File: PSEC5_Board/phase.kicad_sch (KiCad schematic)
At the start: 8 parts, among them U4 SN74LVC1G97DBVTG4, U6 OPA607QDBVRQ1, U7 AD4008BCPZ-RL7, Y1 ASE2-40.000MHZ-ET

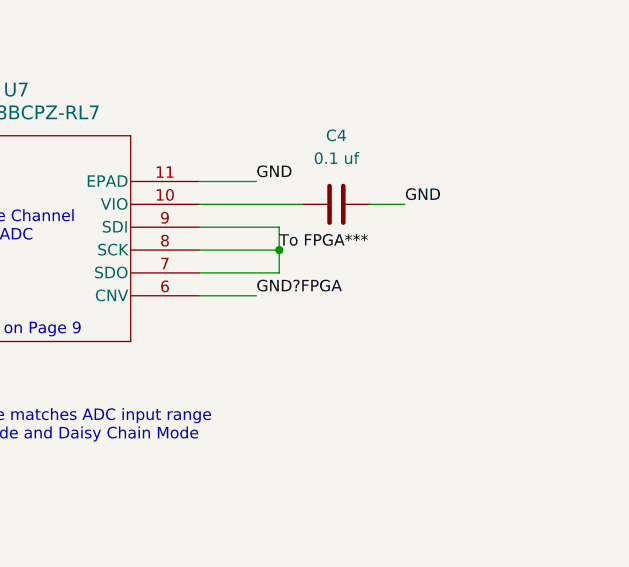
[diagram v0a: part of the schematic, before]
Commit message: DUT Push: ADC Buffer, PLL changes
Implemented ADC Buffer (x1), adjusted PLL ADC.

Missing: PLL DAC, SAMTEC and housekeeping
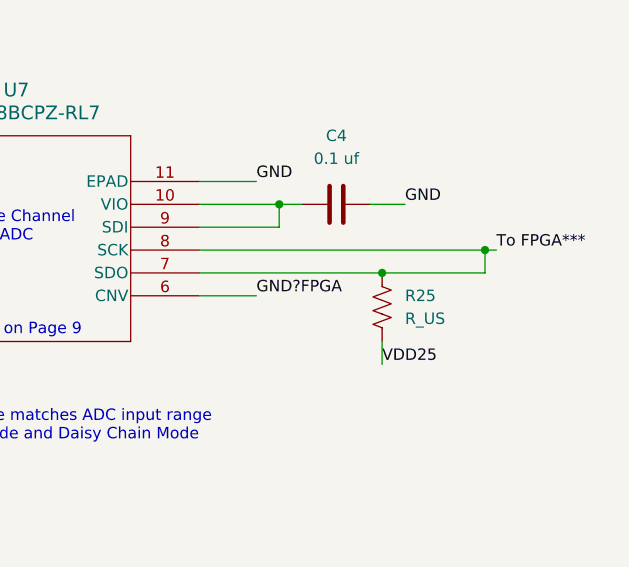
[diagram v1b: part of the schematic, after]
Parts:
- added R25: R_US, symbol Device:R_US
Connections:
- net To FPGA***: now also R25.2; no longer U7.9 (SDI)
- net VDD25: now also R25.1
- net at C4.2, U7.10 (VIO): now also U7.9 (SDI)
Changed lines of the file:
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@@
 	)
 	(junction
-		(at 240.03 91.44)
+		(at 262.89 91.44)
 		(diameter 0)
 		(color 0 0 0 0)
@@
 	)
 	(junction
+		(at 251.46 93.98)
+		(diameter 0)
+		(color 0 0 0 0)
+	)
+	(junction
+		(at 240.03 86.36)
+		(diameter 0)
+		(color 0 0 0 0)
+	)
+	(junction
 		(at 78.74 106.68)
 		(diameter 0)
@@
 	(wire
 		(pts
-			(xy 231.14 86.36) (xy 242.57 86.36)
+			(xy 231.14 86.36) (xy 240.03 86.36)
 		)
 		(stroke
@@
 	(wire
 		(pts
+			(xy 231.14 91.44) (xy 262.89 91.44)
+		)
+		(stroke
+			(width 0)
+			(type default)
+		)
+	)
+	(wire
+		(pts
 			(xy 76.2 106.68) (xy 78.74 106.68)
 		)
@@
 	(wire
 		(pts
-			(xy 240.03 88.9) (xy 240.03 91.44)
-		)
-		(stroke
-			(width 0)
-			(type default)
-		)
-	)
-	(wire
-		(pts
 			(xy 102.87 27.94) (xy 110.49 27.94)
 		)
@@
 	(wire
 		(pts
+			(xy 251.46 93.98) (xy 262.89 93.98)
+		)
+		(stroke
+			(width 0)
+			(type default)
+		)
+	)
+	(wire
+		(pts
 			(xy 179.07 93.98) (xy 190.5 93.98)
 		)
@@
 	(wire
 		(pts
+			(xy 264.16 91.44) (xy 262.89 91.44)
+		)
+		(stroke
+			(width 0)
+			(type default)
+		)
+	)
+	(wire
+		(pts
 			(xy 106.68 147.32) (xy 109.22 147.32)
 		)
@@
 	(wire
 		(pts
-			(xy 231.14 93.98) (xy 240.03 93.98)
+			(xy 231.14 93.98) (xy 251.46 93.98)
 		)
 		(stroke
@@
 	(wire
 		(pts
-			(xy 240.03 93.98) (xy 240.03 91.44)
+			(xy 262.89 91.44) (xy 262.89 93.98)
 		)
 		(stroke
@@
 	(wire
 		(pts
+			(xy 251.46 101.6) (xy 251.46 104.14)
+		)
+		(stroke
+			(width 0)
+			(type default)
+		)
+	)
+	(wire
+		(pts
 			(xy 64.77 166.37) (xy 64.77 153.67)
 		)
@@
 	(wire
 		(pts
+			(xy 240.03 88.9) (xy 240.03 86.36)
+		)
+		(stroke
+			(width 0)
+			(type default)
+		)
+	)
+	(wire
+		(pts
 			(xy 62.23 106.68) (xy 68.58 106.68)
 		)
@@
 	(wire
 		(pts
+			(xy 240.03 86.36) (xy 242.57 86.36)
+		)
+		(stroke
+			(width 0)
+			(type default)
+		)
+	)
+	(wire
+		(pts
 			(xy 97.79 92.71) (xy 102.87 92.71)
 		)
@@
 		(pts
 			(xy 179.07 88.9) (xy 190.5 88.9)
-		)
-		(stroke
-			(width 0)
-			(type default)
-		)
-	)
-	(wire
-		(pts
-			(xy 231.14 91.44) (xy 240.03 91.44)
 		)
 		(stroke
@@
 		)
 	)
+	(label "VDD25"
+		(at 251.46 104.14 0)
+		(fields_autoplaced yes)
+		(effects
+			(font
+				(size 1.27 1.27)
+			)
+			(justify left bottom)
+		)
+	)
 	(label "VDD18?"
 		(at 182.88 86.36 0)
@@
 	)
 	(label "To FPGA***"
-		(at 240.03 91.44 0)
-		(fields_autoplaced yes)
-		(effects
-			(font
-				(size 1.27 1.27)
-			)
-			(justify left bottom)
-		)
-	)
+		(at 264.16 91.44 0)
+		(fields_autoplaced yes)
+		(effects
+			(font
+				(size 1.27 1.27)
+			)
+			(justify left bottom)
+		)
+	)
+	(symbol
+		(lib_id "Device:R_US")
+		(at 251.46 97.79 180)
+		(unit 1)
+		(exclude_from_sim no)
+		(in_bom yes)
+		(on_board yes)
+		(dnp no)
+		(fields_autoplaced yes)
+		(property "Reference" "R25"
+			(at 254 96.5199 0)
+			(effects
+				(font
+					(size 1.27 1.27)
+				)
+				(justify right)
+			)
+		)
+		(property "Value" "R_US"
+			(at 254 99.0599 0)
+			(effects
+				(font
+					(size 1.27 1.27)
+				)
+				(justify right)
+			)
+		)
+		(property "Footprint" ""
+			(at 250.444 97.536 90)
+			(effects
+				(font
+					(size 1.27 1.27)
+				)
+				(hide yes)
+			)
+		)
+		(property "Datasheet" "~"
+			(at 251.46 97.79 0)
+			(effects
+				(font
+					(size 1.27 1.27)
+				)
+				(hide yes)
+			)
+		)
+		(property "Description" "Resistor, US symbol"
+			(at 251.46 97.79 0)
+			(effects
+				(font
+					(size 1.27 1.27)
+				)
+				(hide yes)
+			)
+		)
+		(pin "2"
+		)
+		(pin "1"
+		)
+		(instances
+			(project ""
+				(path "/af906810-6e6b-406e-b884-20eae48a7386/342f9d5e-3615-4623-a80b-f03a940e5896"
+					(reference "R25")
+					(unit 1)
+				)
+			)
+		)
+	)

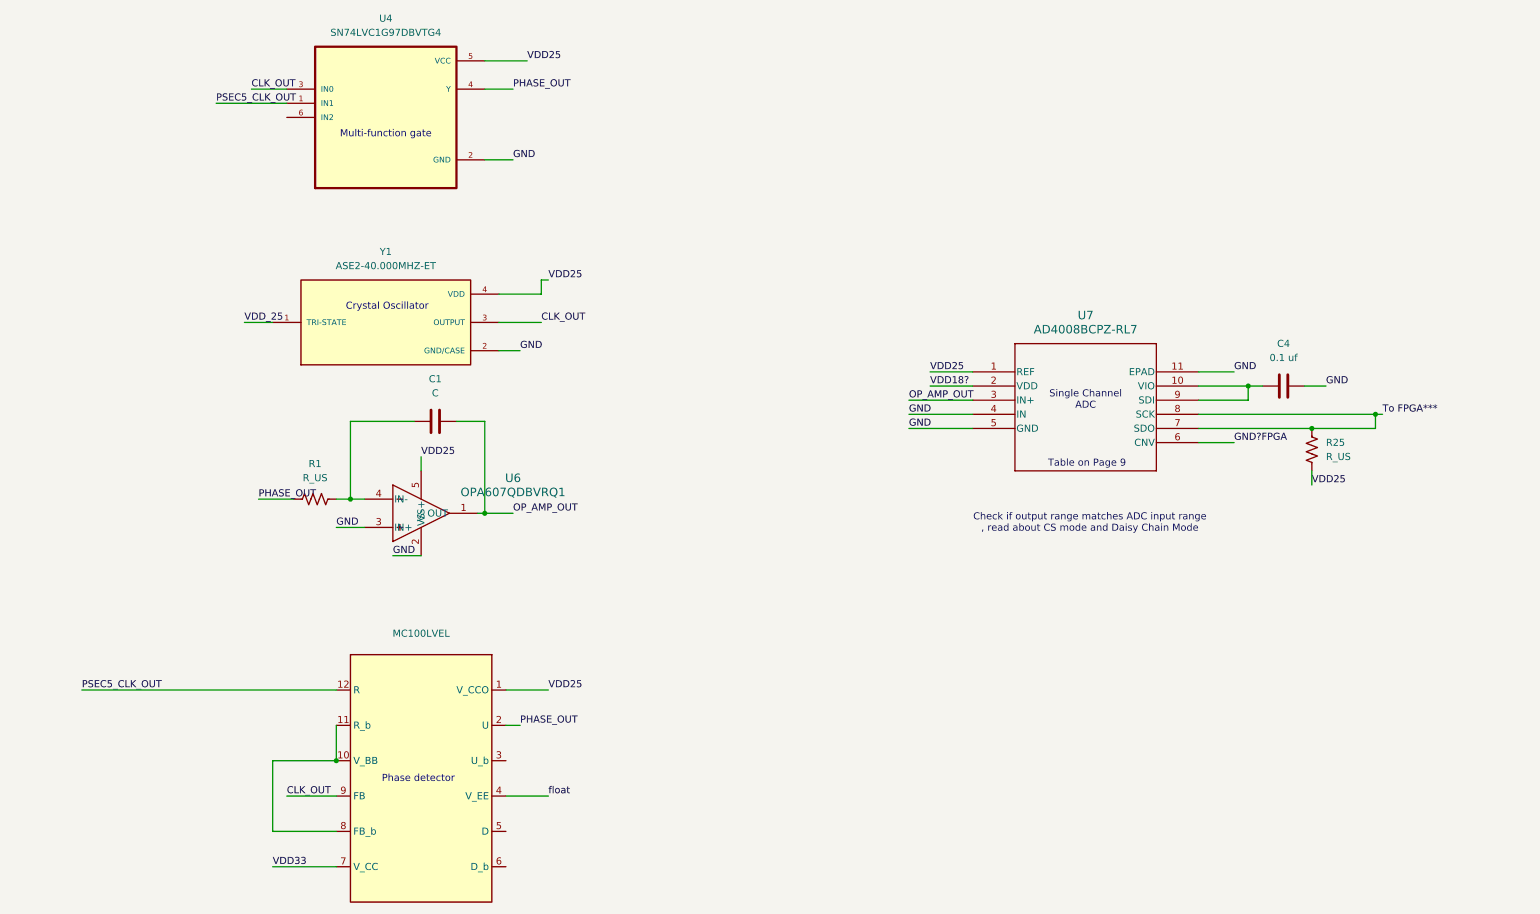
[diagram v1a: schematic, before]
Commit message: DUT Schematic Push
Very close -> Still need to convert to Sheet pins.

Added a second SAMTEC.
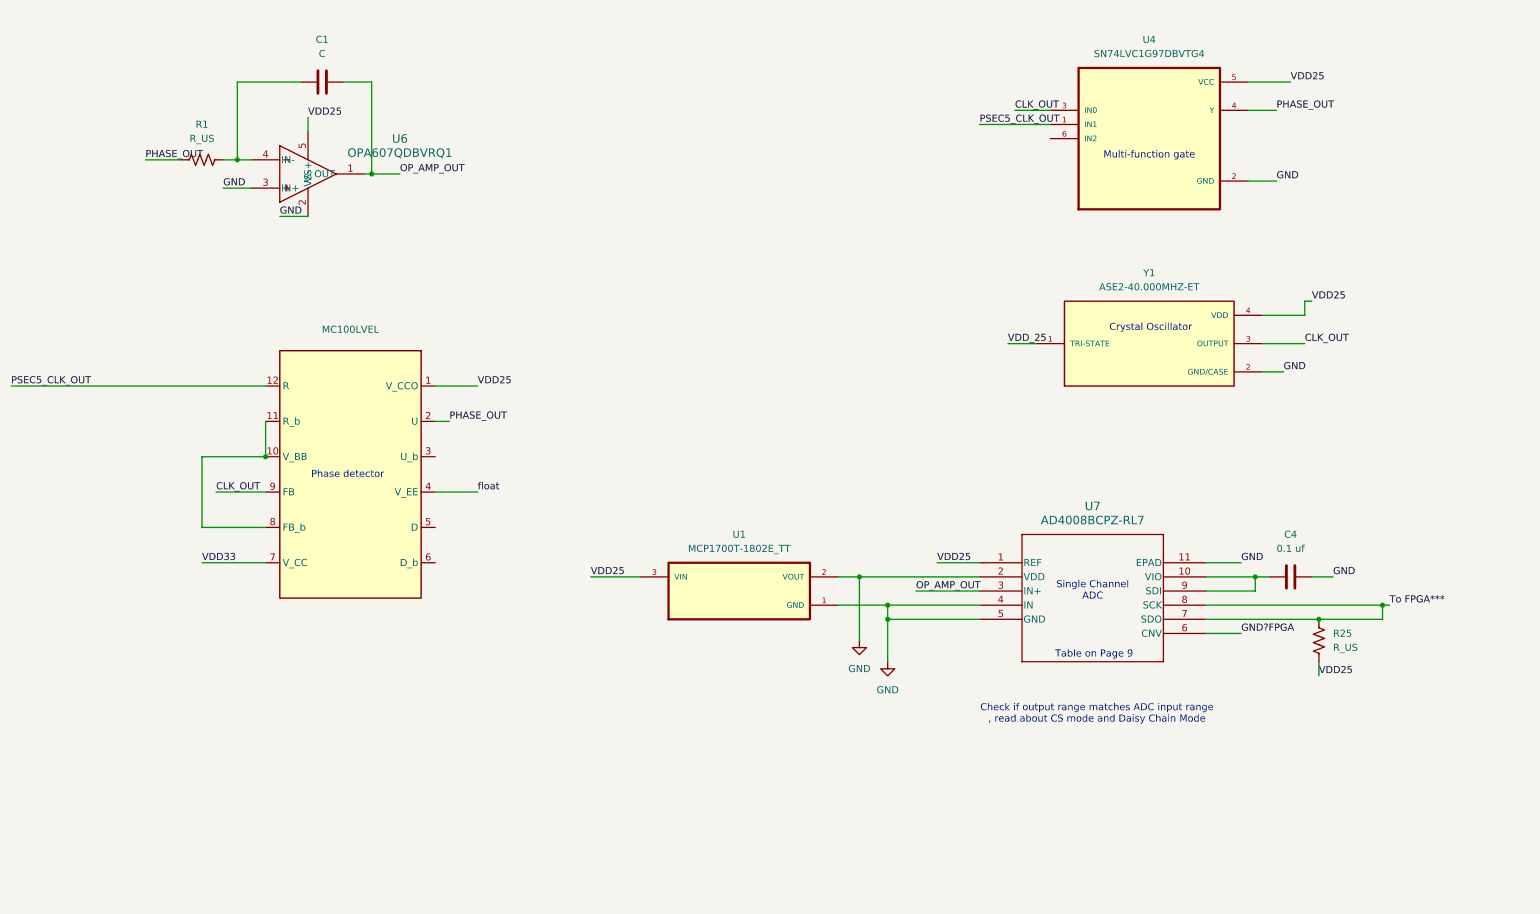
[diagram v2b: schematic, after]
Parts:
- added U1: MCP1700T-1802E_TT, MCP1700T-1802E_TT:SOT95P237X112-3N, symbol MCP1700T-1802E_TT:MCP1700T-1802E_TT
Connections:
- net VDD18? is gone; now on net GND: U7.2 (VDD)
- net GND: now also U1.1 (GND), U1.2 (VOUT)
- net VDD25: now also U1.3 (VIN)
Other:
- moved on the sheet: C1, C4, MC100LVEL, R1, R25, U4, U6, U7, Y1

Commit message: DUT - Fixed ADC Driver
Passes ERC - SAMTEC connections still needs to be matched.
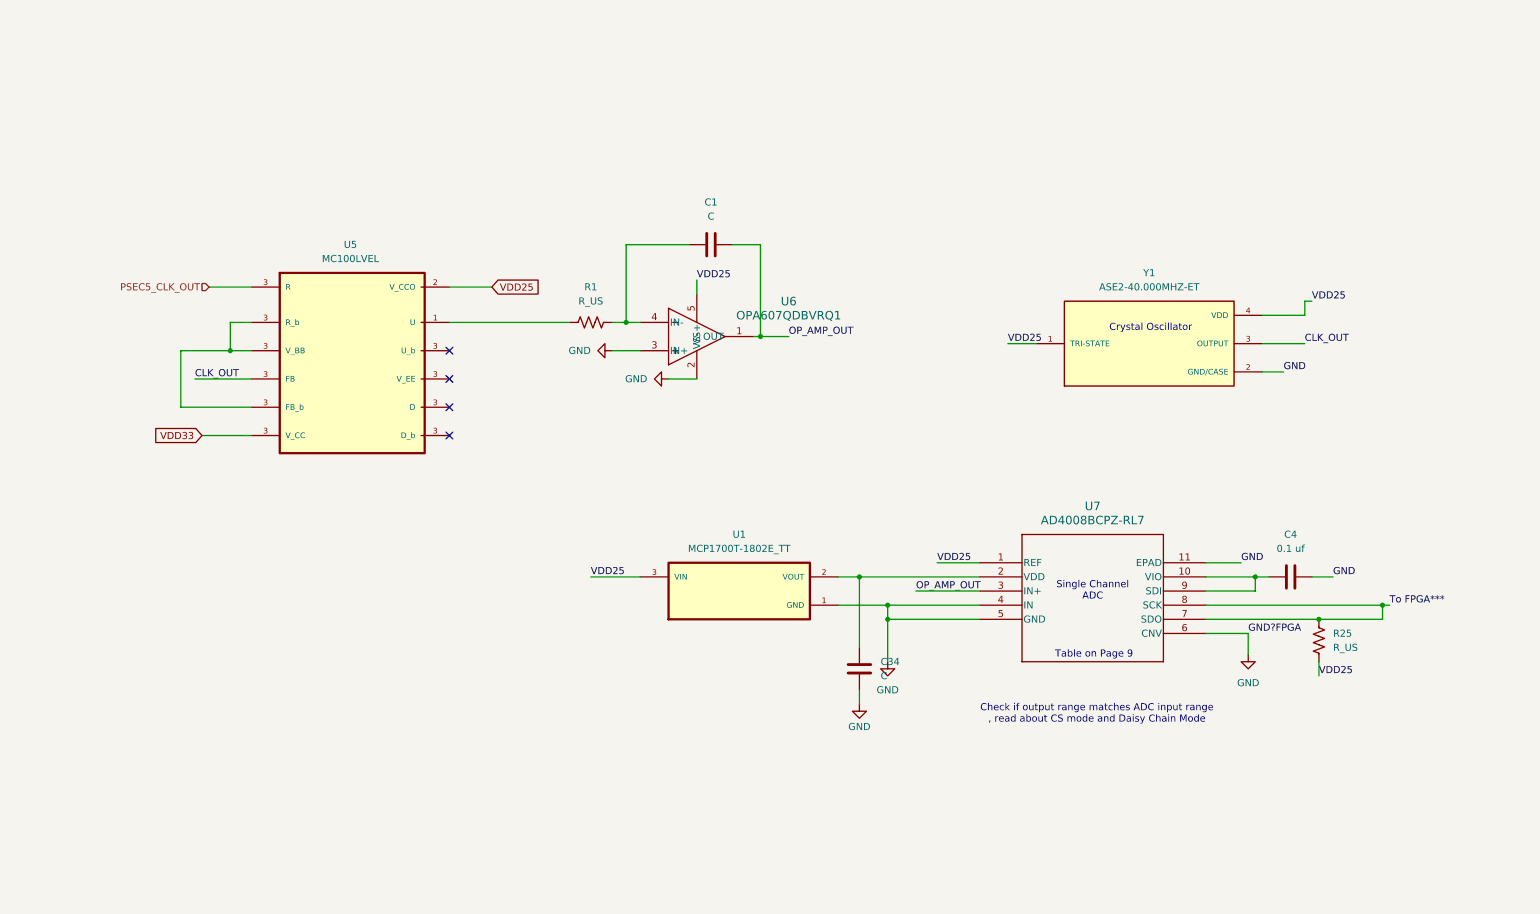
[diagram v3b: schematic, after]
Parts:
- removed MC100LVEL: ~, symbol MC100LVEL40:MC100LVEL40
- removed U4: SN74LVC1G97DBVTG4, SN74LVC1G97DBVTG4:SOT95P280X145-6N, symbol SN74LVC1G97DBVTG4:SN74LVC1G97DBVTG4
- added C34: C, symbol Device:C
- added U5: MC100LVEL, MCP1700T-1802E_TT:SOT95P237X112-3N, symbol MCP1700T-1802E_TT:MCP1700T-1802E_TT
- C1: footprint (none) -> Capacitor_SMD:C_0603_1608Metric
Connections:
- net GND?FPGA is gone; now on net GND: U7.6 (CNV)
- net VDD_25 is gone; now on net VDD25: Y1.1 (TRI-STATE)
- net CLK_OUT: now also U5.3 (V_EE)
- net GND: now also C34.2; no longer U1.2 (VOUT), U7.2 (VDD)
- net PSEC5_CLK_OUT: now also U5.3 (V_EE)
- net VDD25: now also U5.2 (V_CCO)
- net VDD33: now also U5.3 (V_EE)
- net PHASE_OUT: no longer names the net of R1.2
- net PHASE_OUT: now also U5.1 (U)
- new net: C34.1, U1.2 (VOUT), U7.2 (VDD)
- no-connect marks 0 -> 4
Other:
- note removed: "Multi-function gate"
- note removed: "Phase detector"
- moved on the sheet: C1, R1, U6

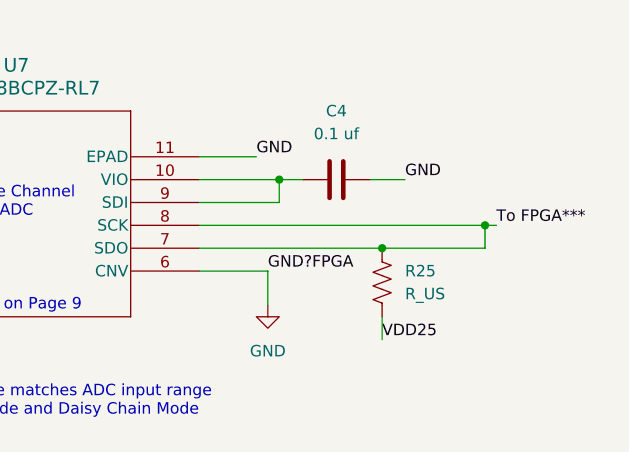
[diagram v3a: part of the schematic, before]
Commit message: DUT adjustments
New Nets in Layout,

Some name changes in Schematic
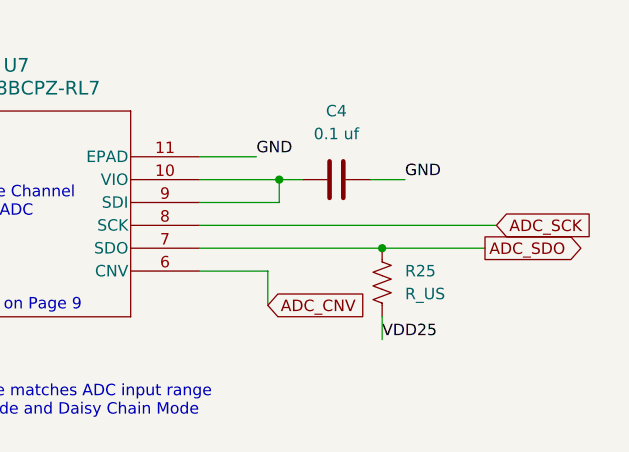
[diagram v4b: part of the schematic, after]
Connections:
- net GND: no longer U7.6 (CNV)
- net To FPGA*** renamed ADC_SDO
- net ADC_SDO: no longer U7.8 (SCK)
- new net ADC_CNV: U7.6 (CNV)
- new net ADC_SCK: U7.8 (SCK)
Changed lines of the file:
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@@
-	)
-	(junction
-		(at 264.16 125.73)
-		(diameter 0)
-		(color 0 0 0 0)
 	)
 	(junction
@@
 	(wire
 		(pts
-			(xy 232.41 125.73) (xy 264.16 125.73)
+			(xy 232.41 125.73) (xy 265.43 125.73)
 		)
 		(stroke
@@
 	(wire
 		(pts
-			(xy 265.43 125.73) (xy 264.16 125.73)
-		)
-		(stroke
-			(width 0)
-			(type default)
-		)
-	)
-	(wire
-		(pts
 			(xy 57.15 74.93) (xy 57.15 80.01)
 		)
@@
 		(pts
 			(xy 242.57 83.82) (xy 246.38 83.82)
-		)
-		(stroke
-			(width 0)
-			(type default)
-		)
-	)
-	(wire
-		(pts
-			(xy 264.16 125.73) (xy 264.16 128.27)
 		)
 		(stroke
@@
 		)
 	)
-	(label "GND?FPGA"
-		(at 240.03 130.81 0)
-		(fields_autoplaced yes)
-		(effects
-			(font
-				(size 1.27 1.27)
-			)
-			(justify left bottom)
-		)
-	)
 	(label "VDD25"
 		(at 140.97 67.31 0)
@@
 	(label "OP_AMP_OUT"
 		(at 180.34 123.19 0)
-		(fields_autoplaced yes)
-		(effects
-			(font
-				(size 1.27 1.27)
-			)
-			(justify left bottom)
-		)
-	)
-	(label "To FPGA***"
-		(at 265.43 125.73 0)
 		(fields_autoplaced yes)
 		(effects
@@
 		)
 	)
+	(global_label "ADC_CNV"
+		(shape input)
+		(at 240.03 134.62 0)
+		(fields_autoplaced yes)
+		(effects
+			(font
+				(size 1.27 1.27)
+			)
+			(justify left)
+		)
+		(property "Intersheetrefs" "${INTERSHEET_REFS}"
+			(at 251.3005 134.62 0)
+			(effects
+				(font
+					(size 1.27 1.27)
+				)
+				(justify left)
+				(hide yes)
+			)
+		)
+	)
 	(global_label "VDD25"
 		(shape input)
@@
 		(property "Intersheetrefs" "${INTERSHEET_REFS}"
 			(at 113.1728 68.58 0)
+			(effects
+				(font
+					(size 1.27 1.27)
+				)
+				(justify left)
+				(hide yes)
+			)
+		)
+	)
+	(global_label "ADC_SDO"
+		(shape output)
+		(at 264.16 128.27 0)
+		(fields_autoplaced yes)
+		(effects
+			(font
+				(size 1.27 1.27)
+			)
+			(justify left)
+		)
+		(property "Intersheetrefs" "${INTERSHEET_REFS}"
+			(at 275.5514 128.27 0)
+			(effects
+				(font
+					(size 1.27 1.27)
+				)
+				(justify left)
+				(hide yes)
+			)
+		)
+	)
+	(global_label "ADC_SCK"
+		(shape input)
+		(at 265.43 125.73 0)
+		(fields_autoplaced yes)
+		(effects
+			(font
+				(size 1.27 1.27)
+			)
+			(justify left)
+		)
+		(property "Intersheetrefs" "${INTERSHEET_REFS}"
+			(at 276.7609 125.73 0)
 			(effects
 				(font
@@
 					(unit 1)
 				)
-			)
-		)
-	)
-	(symbol
-		(lib_id "power:GND")
-		(at 240.03 134.62 0)
-		(unit 1)
-		(exclude_from_sim no)
-		(in_bom yes)
-		(on_board yes)
-		(dnp no)
-		(fields_autoplaced yes)
-		(property "Reference" "#PWR039"
-			(at 240.03 140.97 0)
-			(effects
-				(font
-					(size 1.27 1.27)
-				)
-				(hide yes)
-			)
-		)
-		(property "Value" "GND"
-			(at 240.03 139.7 0)
-			(effects
-				(font
-					(size 1.27 1.27)
-				)
-			)
-		)
-		(property "Footprint" ""
-			(at 240.03 134.62 0)
-			(effects
-				(font
-					(size 1.27 1.27)
-				)
-				(hide yes)
-			)
-		)
-		(property "Datasheet" ""
-			(at 240.03 134.62 0)
-			(effects
-				(font
-					(size 1.27 1.27)
-				)
-				(hide yes)
-			)
-		)
-		(property "Description" "Power symbol creates a global label with name \"GND\" , ground"
-			(at 240.03 134.62 0)
-			(effects
-				(font
-					(size 1.27 1.27)
-				)
-				(hide yes)
-			)
-		)
-		(pin "1"
-		)
-		(instances
-			(project ""
-				(path "/af906810-6e6b-406e-b884-20eae48a7386/342f9d5e-3615-4623-a80b-f03a940e5896"
-					(reference "#PWR039")
-					(unit 1)
-				)

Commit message: Added Footprints to Schematic
Added footprints to schematic, should be able to now update the layout design and have all nets be present
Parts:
- C34, C4, R25: footprint (none) -> Capacitor_SMD:C_0603_1608Metric
- R1: footprint (none) -> Resistor_SMD:R_0603_1608Metric
- U1, U5: footprint MCP1700T-1802E_TT:SOT95P237X112-3N -> MCP1700T_1802E_TT:SOT95P237X112-3N
- U6: footprint DBV0005A-IPC_A -> footprints:DBV0005A-IPC_A
- U7: footprint CP_10_9_ADI -> AD4008BCPZ-RL7:CP_10_9_ADI
- Y1: footprint ASE2-40.000MHZ-ET:XTAL_ASE2-40.000MHZ-ET -> ASE2_40_000MHZ_E_T:XTAL_ASE2-40.000MHZ-ET
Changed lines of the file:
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@@
 			)
 		)
-		(property "Footprint" ""
+		(property "Footprint" "Capacitor_SMD:C_0603_1608Metric"
 			(at 251.714 131.826 90)
 			(effects
@@
 			)
 		)
-		(property "Footprint" "ASE2-40.000MHZ-ET:XTAL_ASE2-40.000MHZ-ET"
+		(property "Footprint" "ASE2_40_000MHZ_E_T:XTAL_ASE2-40.000MHZ-ET"
 			(at 222.25 78.74 0)
 			(effects
@@
 			)
 		)
-		(property "Footprint" "CP_10_9_ADI"
+		(property "Footprint" "AD4008BCPZ-RL7:CP_10_9_ADI"
 			(at 191.77 118.11 0)
 			(effects
@@
 			)
 		)
-		(property "Footprint" ""
+		(property "Footprint" "Capacitor_SMD:C_0603_1608Metric"
 			(at 243.84 121.6152 0)
 			(effects
@@
 			)
 		)
-		(property "Footprint" ""
+		(property "Footprint" "Capacitor_SMD:C_0603_1608Metric"
 			(at 171.1452 140.97 0)
 			(effects
@@
 			)
 		)
-		(property "Footprint" "MCP1700T-1802E_TT:SOT95P237X112-3N"
+		(property "Footprint" "MCP1700T_1802E_TT:SOT95P237X112-3N"
 			(at 148.59 123.19 0)
 			(effects
@@
 			)
 		)
-		(property "Footprint" ""
+		(property "Footprint" "Resistor_SMD:R_0603_1608Metric"
 			(at 121.666 75.946 90)
 			(effects
@@
 			)
 		)
-		(property "Footprint" "MCP1700T-1802E_TT:SOT95P237X112-3N"
+		(property "Footprint" "MCP1700T_1802E_TT:SOT95P237X112-3N"
 			(at 78.74 71.12 0)
 			(effects
@@
 			)
 		)
-		(property "Footprint" "DBV0005A-IPC_A"
+		(property "Footprint" "footprints:DBV0005A-IPC_A"
 			(at 130.81 74.93 0)
 			(effects
